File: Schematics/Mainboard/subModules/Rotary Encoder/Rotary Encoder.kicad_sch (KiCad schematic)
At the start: 7 parts, among them J1 Power, J2 Data, SW1 Rot

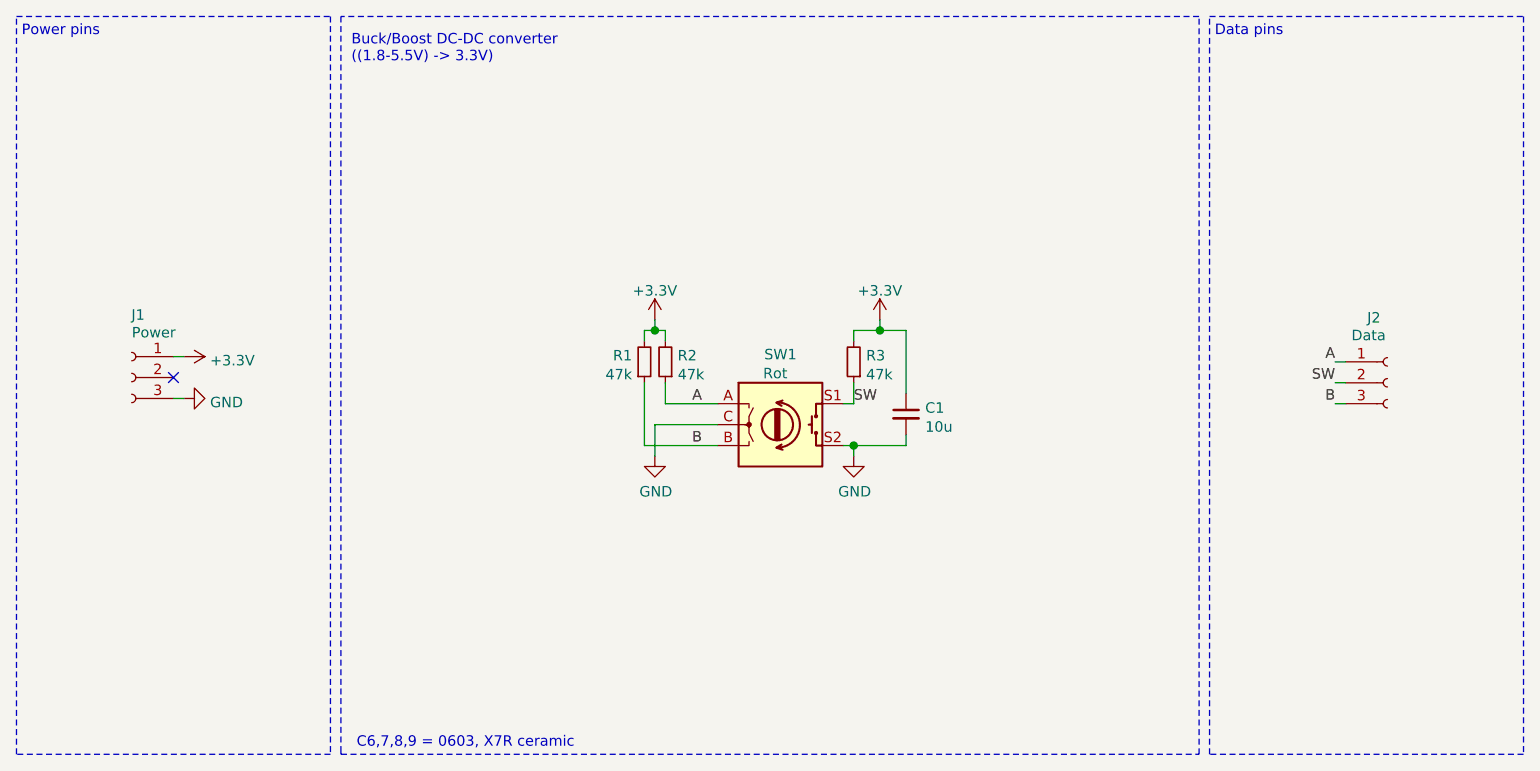
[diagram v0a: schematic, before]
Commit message: Added schematic + PCB for rot enc
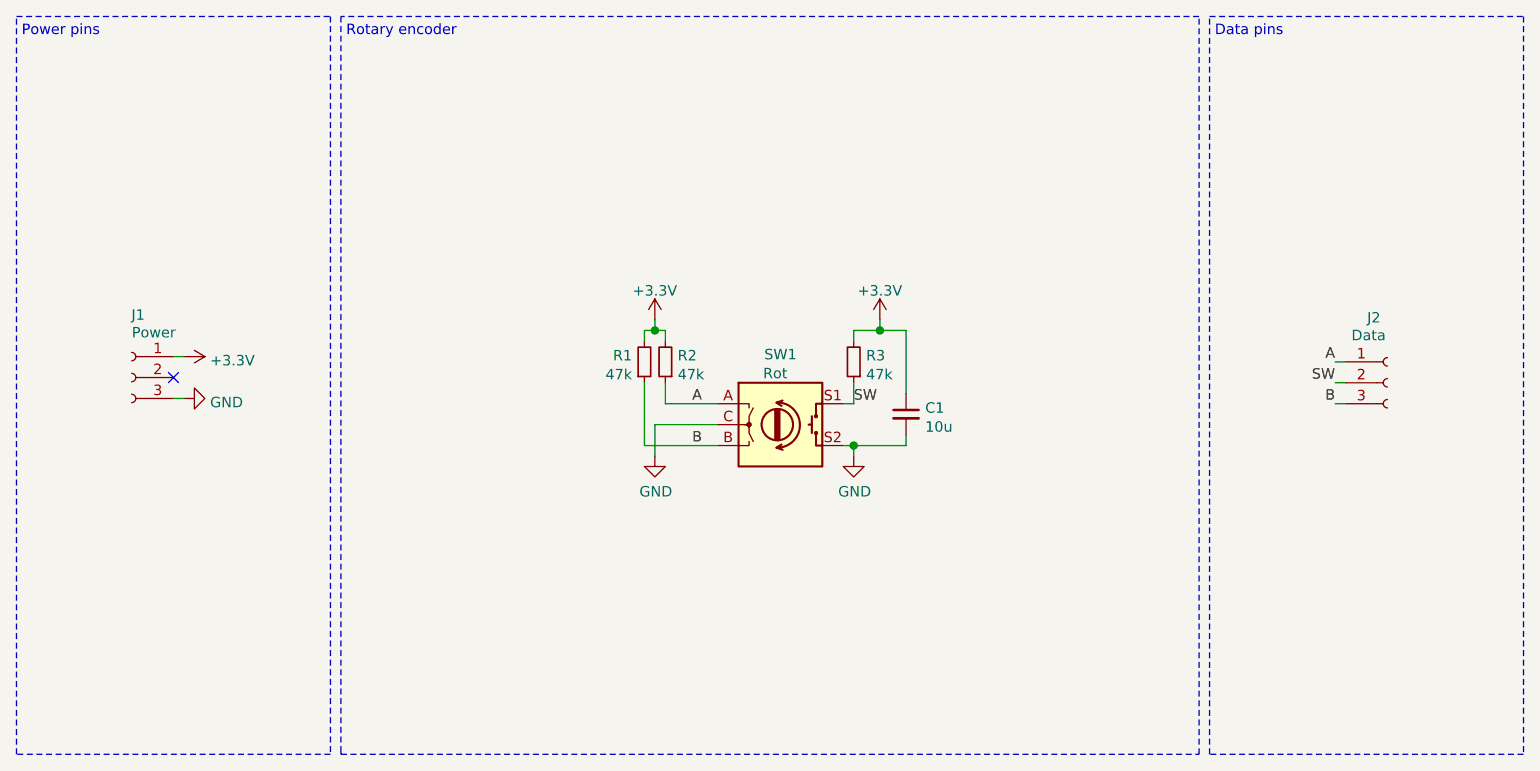
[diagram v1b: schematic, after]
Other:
- note added: "Rotary encoder"
- note removed: "Buck/Boost DC-DC converter ((1.8-5.5V) -> 3.3V)"
- note removed: "C6,7,8,9 = 0603, X7R ceramic"
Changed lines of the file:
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@@
     (effects (font (size 1.27 1.27)) (justify left bottom))
   )
-  (text "Buck/Boost DC-DC converter\n((1.8-5.5V) -> 3.3V)" (at 53.975 19.05 0)
+  (text "Rotary encoder" (at 53.34 15.875 0)
     (effects (font (size 1.27 1.27)) (justify left bottom))
   )
-  (text "C6,7,8,9 = 0603, X7R ceramic" (at 54.61 102.235 0)
-    (effects (font (size 1.27 1.27)) (justify left bottom))
-  )

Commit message: Added files for rotary encoder prod
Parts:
- C1: LCSC Part (none) -> C19702
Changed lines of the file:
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@@
+      (effects (font (size 1.27 1.27)) hide)
+    )
+    (property "LCSC Part" "C19702" (id 4) (at 121.285 61.595 0)
       (effects (font (size 1.27 1.27)) hide)
     )
